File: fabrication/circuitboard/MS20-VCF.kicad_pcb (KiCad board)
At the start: 2 copper layers, 60 x 110 mm, 79 parts, among them J13 Conn_CircuitBoard, J3 Conn_CircuitBoard, J6 Conn_CircuitBoard, J8 Power Input, J9 Conn_CircuitBoard, Q1 BC559, Q2 BC559, Q3 BC559, Q4 BC559, U1 LM13700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

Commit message: update worflow run condition + trimmer footprint update
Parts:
- C1, C15: value 10µF -> 10uF
- C10, C5: value 10µ -> 10uF
- ResLv1: value 5k -> 10k; footprint Potentiometer_THT:Potentiometer_Bourns_3386X_Horizontal -> Potentiometer_THT:Potentiometer_Bourns_3386C_Horizontal
- ResLv2, ResVol1, ResVol2: footprint Potentiometer_THT:Potentiometer_Bourns_3386X_Horizontal -> Potentiometer_THT:Potentiometer_Bourns_3386C_Horizontal
- moved ResVol2 1.30 mm to (87.3, 93.8)
- moved ResLv1 1.30 mm to (87.3, 55.6)
- moved ResLv2 1.30 mm to (87.3, 103.9)
- moved ResVol1 1.30 mm to (87.3, 45.4)
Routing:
- net Net-(C2-Pad2): track 43.5 -> 47.0 mm
- net Net-(C16-Pad2): track 52.8 -> 55.2 mm
- net Net-(D3-Pad1): track 38.4 -> 40.2 mm
- net Net-(D10-Pad1): track 31.1 -> 32.9 mm
- net Net-(D1-Pad2): track 5.76 -> 7.06 mm
- net Net-(D11-Pad1): track 12.0 -> 13.3 mm

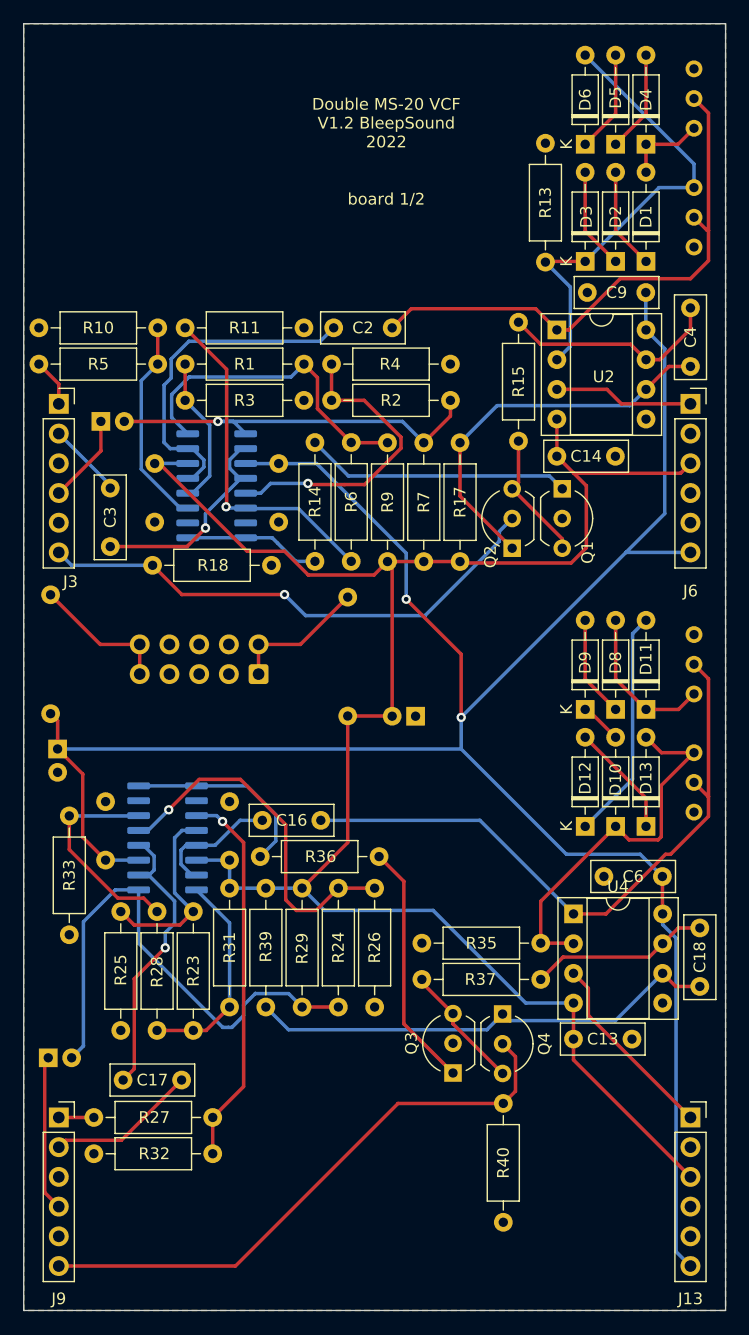
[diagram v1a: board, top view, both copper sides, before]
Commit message: update front panel and infos on components
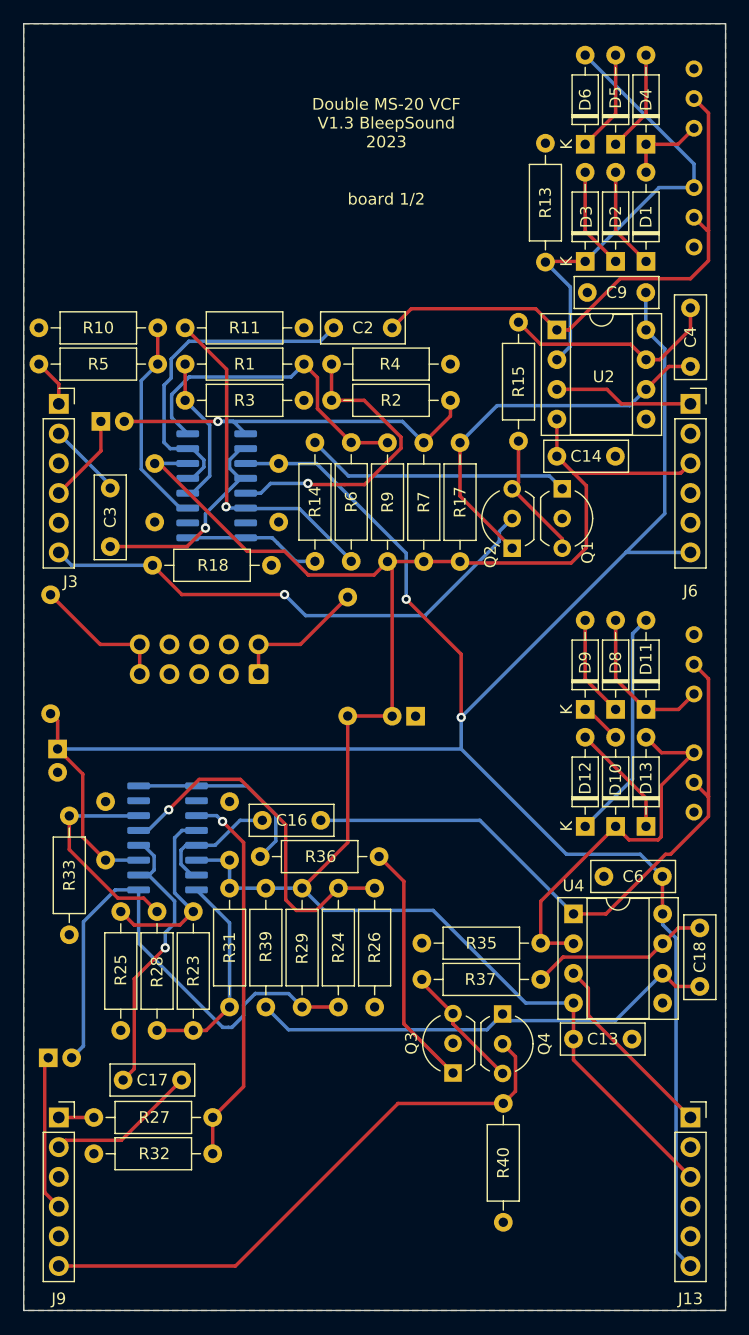
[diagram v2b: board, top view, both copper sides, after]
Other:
- board text added: "Double MS-20 VCF V1.3 BleepSound 2023"
- board text removed: "Double MS-20 VCF V1.2 BleepSound 2022"

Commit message: update documentation + update repo layout
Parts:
- ResLv2: value 3.3k -> 10k

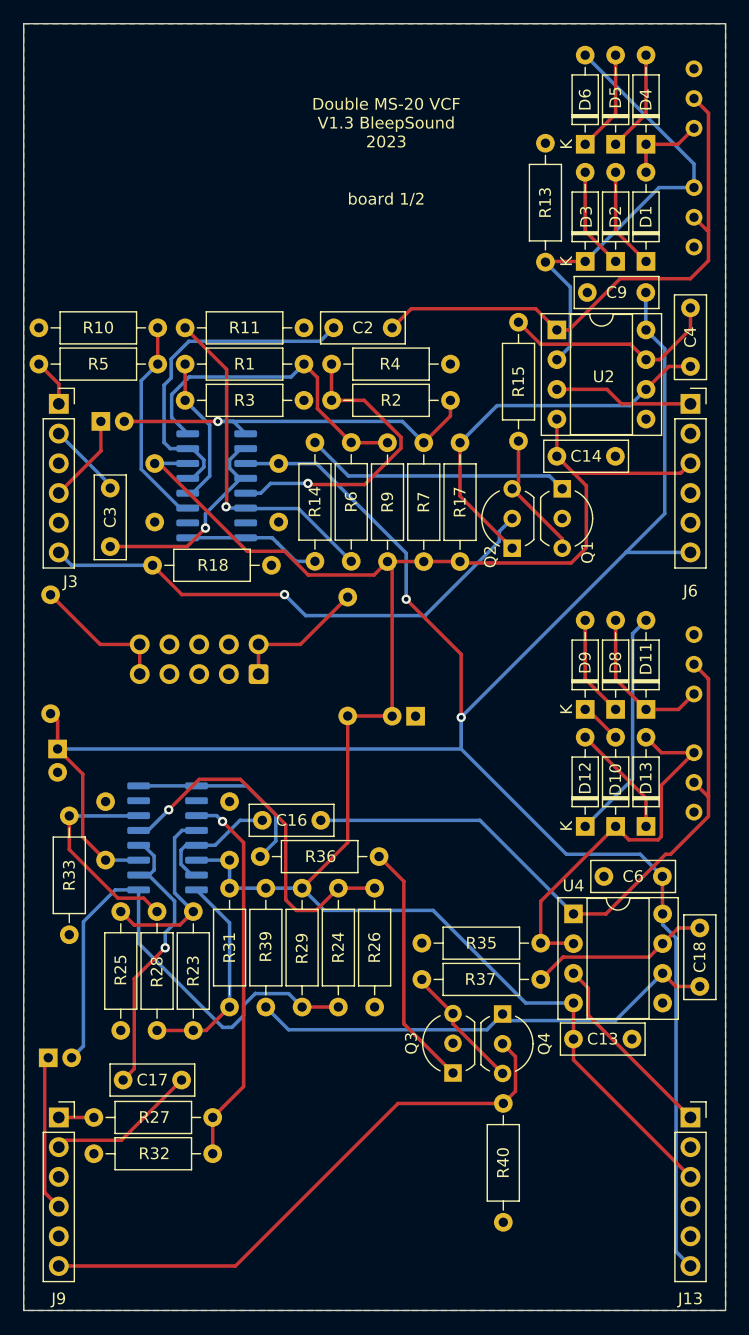
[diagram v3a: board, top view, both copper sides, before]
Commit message: V2.0
new front panel layout
new normalisation for CV and in/out for bandpass filter
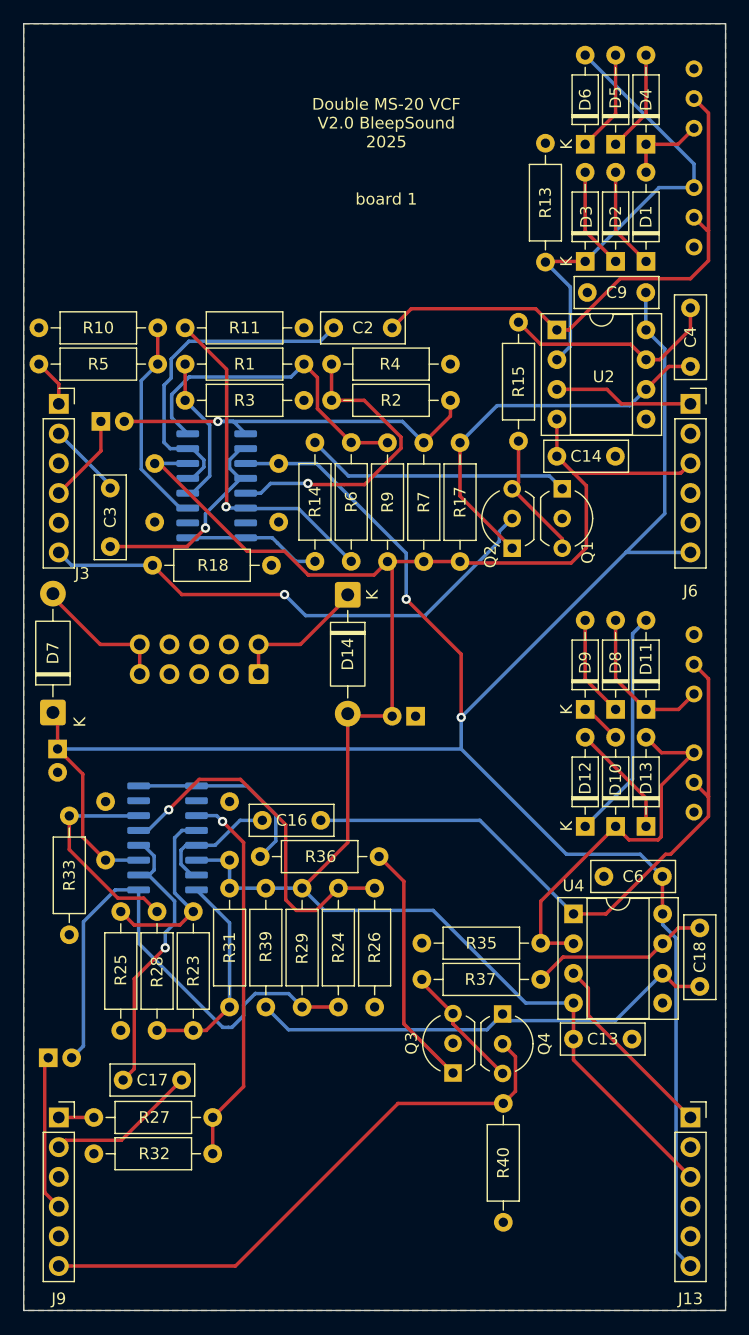
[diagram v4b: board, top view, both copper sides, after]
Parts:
- removed FB1, FB2: 10R, Inductor_THT:L_Axial_L7.0mm_D3.3mm_P10.16mm_Horizontal_Fastron_MICC
- added D14: 1N5819, Diode_THT:D_DO-41_SOD81_P10.16mm_Horizontal, F.Cu at (57.7, 85.3)
- added D7: 1N5819, Diode_THT:D_DO-41_SOD81_P10.16mm_Horizontal, F.Cu at (32.5, 95.4)
- ResLv1, ResLv2, ResVol1, ResVol2: footprint Potentiometer_THT:Potentiometer_Bourns_3386C_Horizontal -> Potentiometer_THT:Potentiometer_Bourns_3296W_Vertical
- turned ResLv1 to -90 degrees
- turned ResLv2 to -90 degrees
- turned ResVol1 to -90 degrees
- turned ResVol2 to -90 degrees
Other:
- board text added: "Double MS-20 VCF V2.0 BleepSound 2025"
- board text added: "board 1"
- board text removed: "Double MS-20 VCF V1.3 BleepSound 2023"
- board text removed: "board 1/2"
